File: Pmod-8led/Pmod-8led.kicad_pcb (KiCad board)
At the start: 2 copper layers, 24 x 16 mm, 18 parts

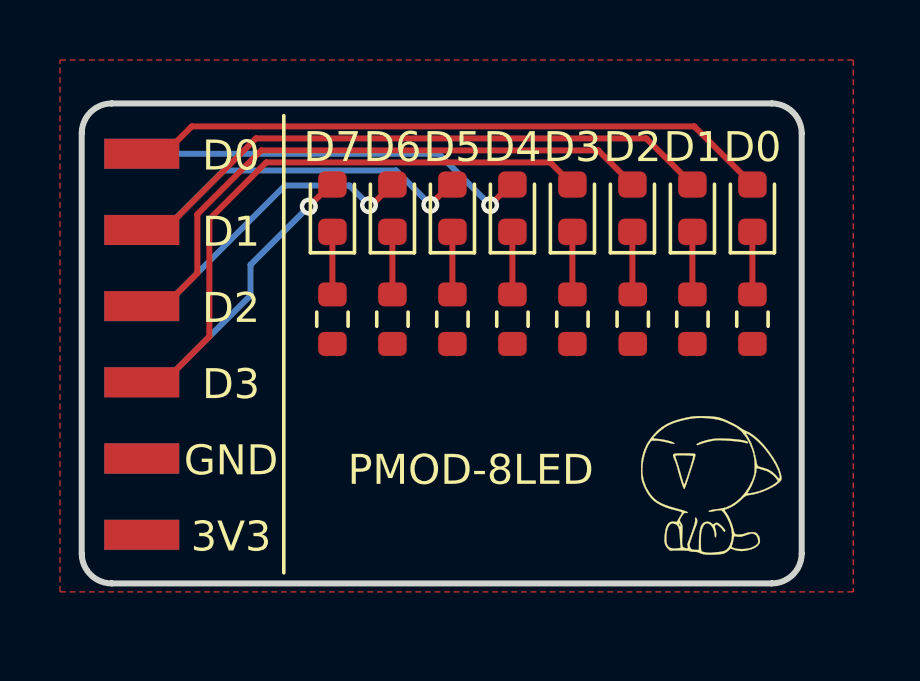
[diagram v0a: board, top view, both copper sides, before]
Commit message: add silk screen
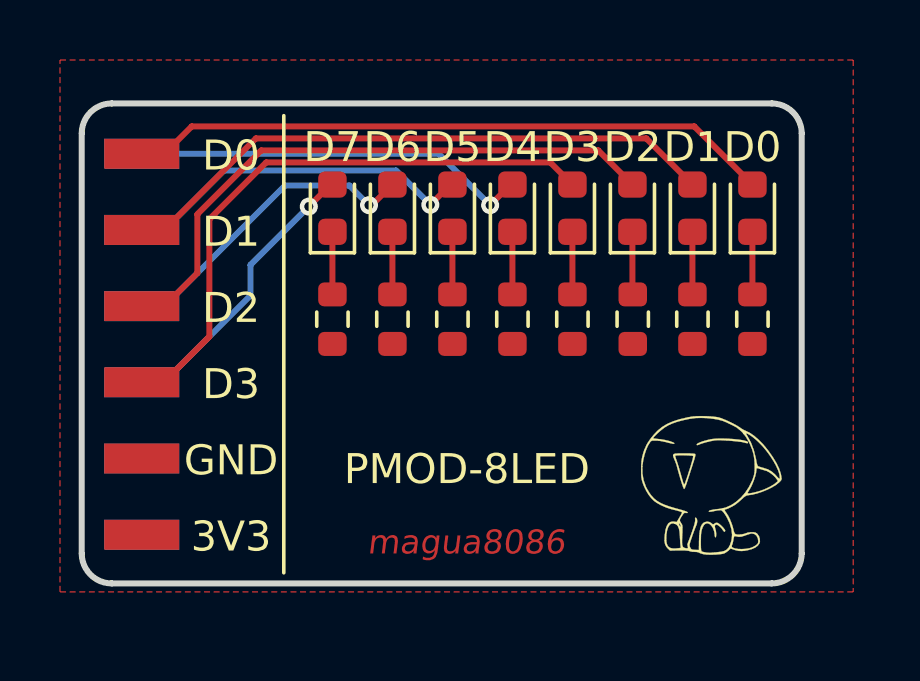
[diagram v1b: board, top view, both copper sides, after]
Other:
- board text added: "magua8086"

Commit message: update PCB
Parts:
- moved G*** 0.51 mm to (167.1, 108.3)
- moved R0 0.40 mm to (169.0, 103.3)
- moved R1 0.40 mm to (167.0, 103.3)
- moved R2 0.40 mm to (165.0, 103.3)
- moved R3 0.40 mm to (163.0, 103.3)
- moved R4 0.40 mm to (161.0, 103.3)
- moved R5 0.40 mm to (159.0, 103.3)
- moved R6 0.40 mm to (157.0, 103.3)
- moved R7 0.40 mm to (155.0, 103.3)
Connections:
- PMOD0 pad 12: +3V3 -> Net-(PMOD0-Pad12)
- PMOD0 pad 6: +3V3 -> Net-(PMOD0-Pad6)
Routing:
- net GND: vias 0 -> 2
- added copper zone on B.Cu, net GND
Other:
- board text added: "Ver: 1.1 2021.8.15 magua8086"
- board text removed: "Ver: 1.0 2021.8.11 magua8086"
